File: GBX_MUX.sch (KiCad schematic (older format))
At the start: 14 parts, among them SW4 SW_DIPTRONICS_DHA-04TQ, U44 PI3DBS12212AZBSEX, U45 PI3DBS12212AZBSEX, U46 PI3DBS12212AZBSEX

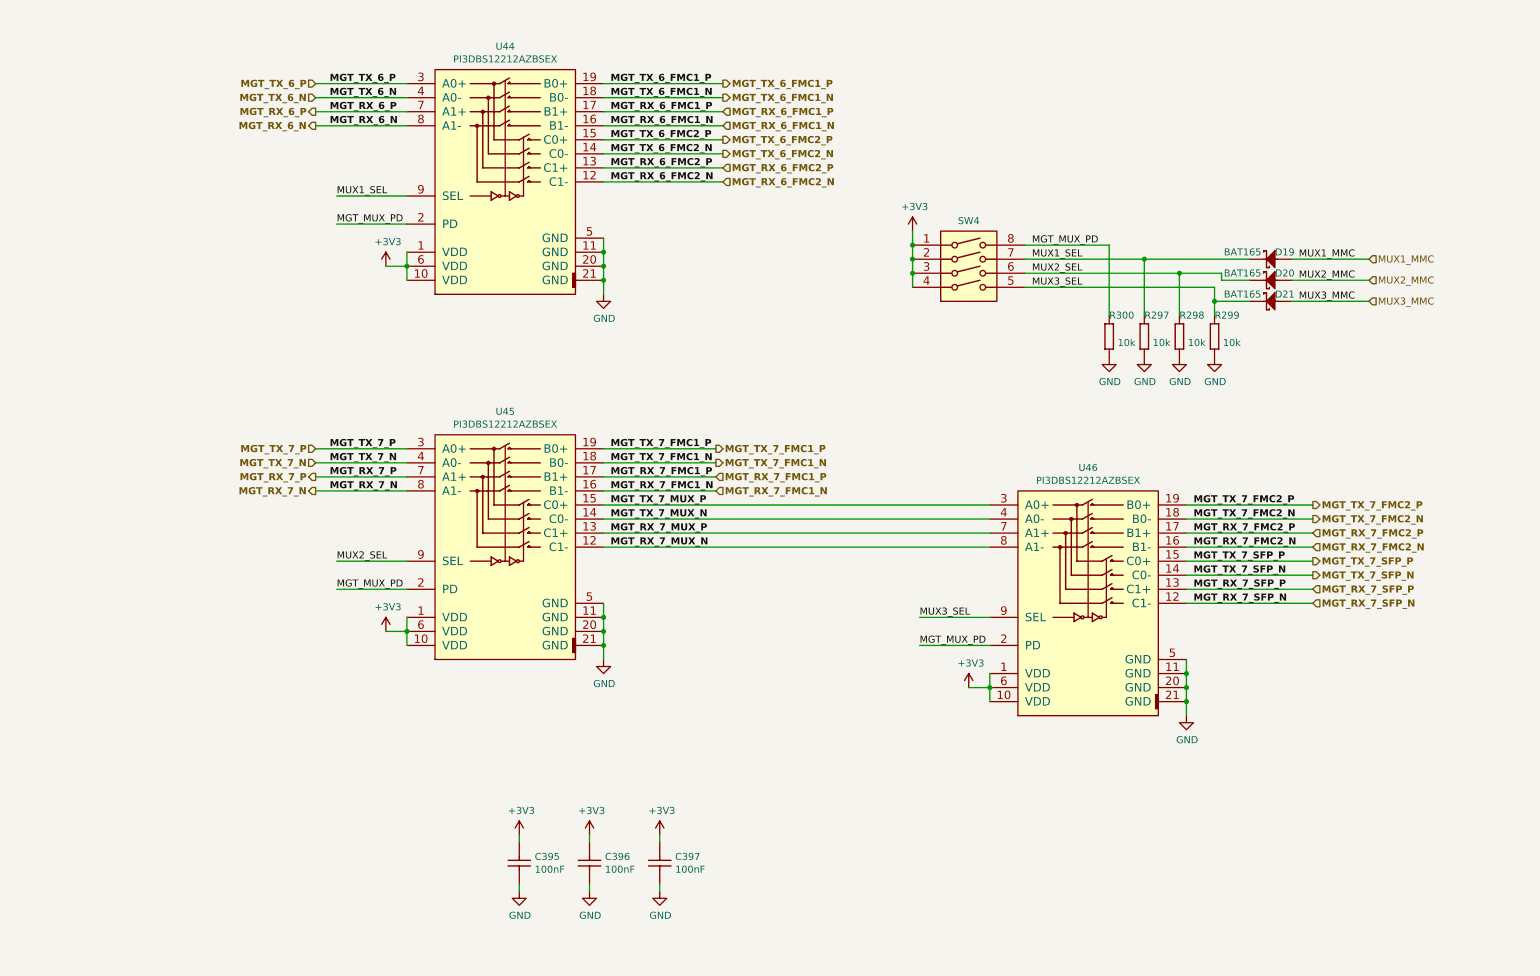
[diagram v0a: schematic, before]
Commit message: FMC HPC & LPC done, FPGA power delivery done, RGMII lines done,  MGT lines progress
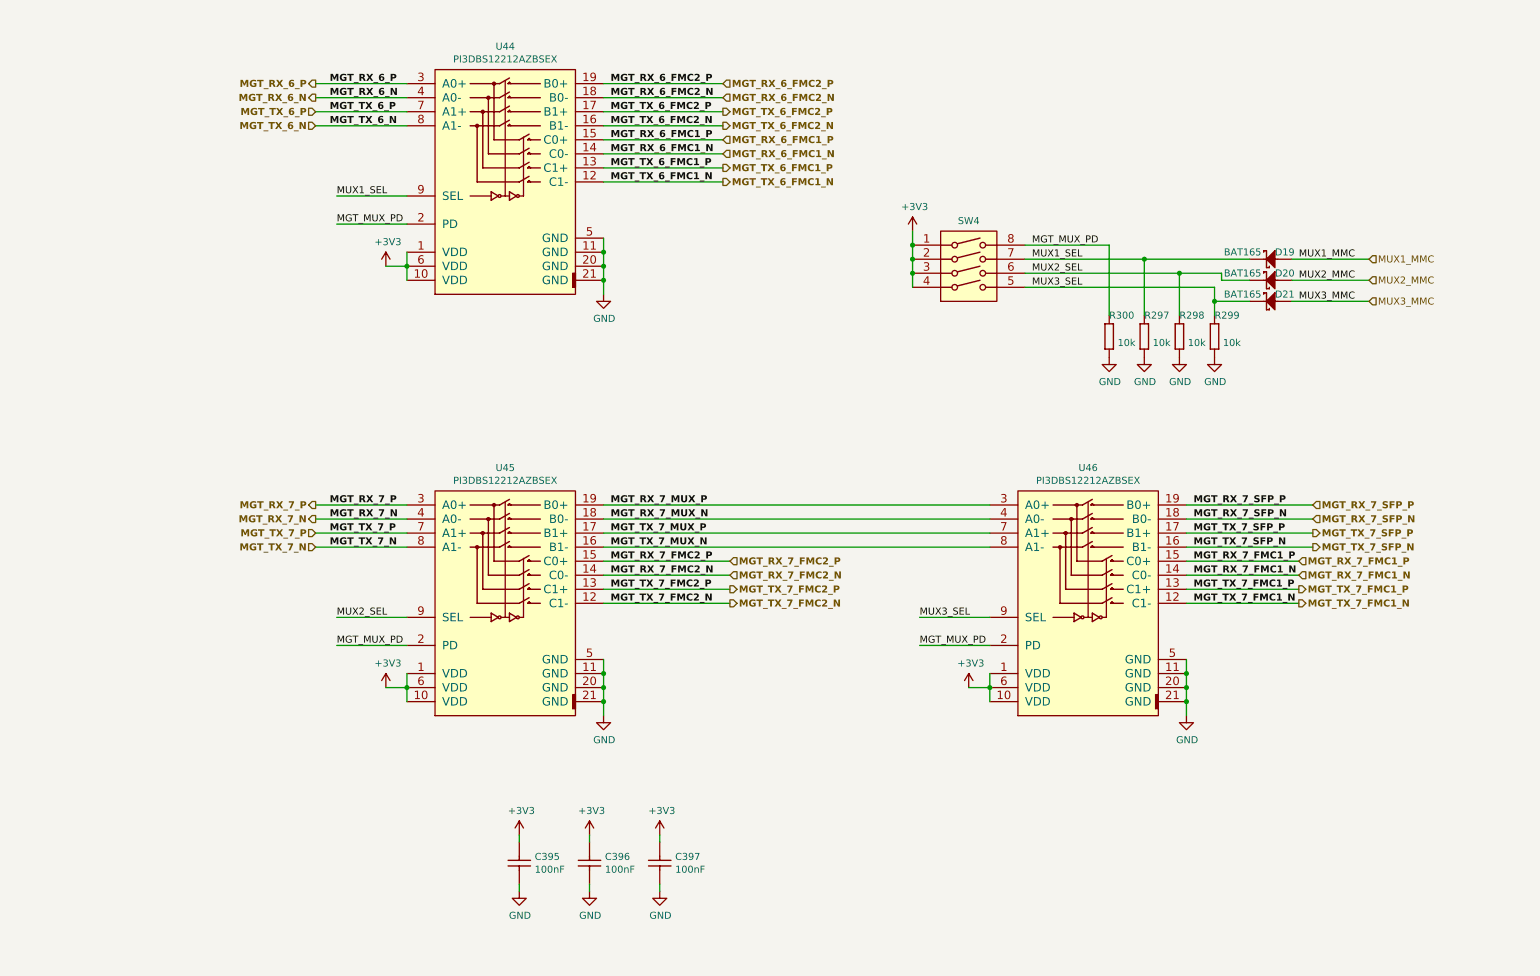
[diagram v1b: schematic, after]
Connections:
- net MGT_RX_6_FMC1_N: now also U44.14 (C0-); no longer U44.16 (B1-)
- net MGT_RX_6_FMC1_P: now also U44.15 (C0+); no longer U44.17 (B1+)
- net MGT_RX_6_FMC2_N: now also U44.18 (B0-); no longer U44.12 (C1-)
- net MGT_RX_6_FMC2_P: now also U44.19 (B0+); no longer U44.13 (C1+)
- net MGT_RX_6_N: now also U44.4 (A0-); no longer U44.8 (A1-)
- net MGT_RX_6_P: now also U44.3 (A0+); no longer U44.7 (A1+)
- net MGT_RX_7_FMC1_N: now also U46.14 (C0-); no longer U45.16 (B1-)
- net MGT_RX_7_FMC1_P: now also U46.15 (C0+); no longer U45.17 (B1+)
- net MGT_RX_7_FMC2_N: now also U45.14 (C0-); no longer U46.16 (B1-)
- net MGT_RX_7_FMC2_P: now also U45.15 (C0+); no longer U46.17 (B1+)
- net MGT_RX_7_MUX_N: now also U45.18 (B0-), U46.4 (A0-); no longer U45.12 (C1-), U46.8 (A1-)
- net MGT_RX_7_MUX_P: now also U45.19 (B0+), U46.3 (A0+); no longer U45.13 (C1+), U46.7 (A1+)
- net MGT_RX_7_N: now also U45.4 (A0-); no longer U45.8 (A1-)
- net MGT_RX_7_P: now also U45.3 (A0+); no longer U45.7 (A1+)
- net MGT_RX_7_SFP_N: now also U46.18 (B0-); no longer U46.12 (C1-)
- net MGT_RX_7_SFP_P: now also U46.19 (B0+); no longer U46.13 (C1+)
- net MGT_TX_6_FMC1_N: now also U44.12 (C1-); no longer U44.18 (B0-)
- net MGT_TX_6_FMC1_P: now also U44.13 (C1+); no longer U44.19 (B0+)
- net MGT_TX_6_FMC2_N: now also U44.16 (B1-); no longer U44.14 (C0-)
- net MGT_TX_6_FMC2_P: now also U44.17 (B1+); no longer U44.15 (C0+)
- net MGT_TX_6_N: now also U44.8 (A1-); no longer U44.4 (A0-)
- net MGT_TX_6_P: now also U44.7 (A1+); no longer U44.3 (A0+)
- net MGT_TX_7_FMC1_N: now also U46.12 (C1-); no longer U45.18 (B0-)
- net MGT_TX_7_FMC1_P: now also U46.13 (C1+); no longer U45.19 (B0+)
- net MGT_TX_7_FMC2_N: now also U45.12 (C1-); no longer U46.18 (B0-)
- net MGT_TX_7_FMC2_P: now also U45.13 (C1+); no longer U46.19 (B0+)
- net MGT_TX_7_MUX_N: now also U45.16 (B1-), U46.8 (A1-); no longer U45.14 (C0-), U46.4 (A0-)
- net MGT_TX_7_MUX_P: now also U45.17 (B1+), U46.7 (A1+); no longer U45.15 (C0+), U46.3 (A0+)
- net MGT_TX_7_N: now also U45.8 (A1-); no longer U45.4 (A0-)
- net MGT_TX_7_P: now also U45.7 (A1+); no longer U45.3 (A0+)
- net MGT_TX_7_SFP_N: now also U46.16 (B1-); no longer U46.14 (C0-)
- net MGT_TX_7_SFP_P: now also U46.17 (B1+); no longer U46.15 (C0+)
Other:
- moved on the sheet: U45

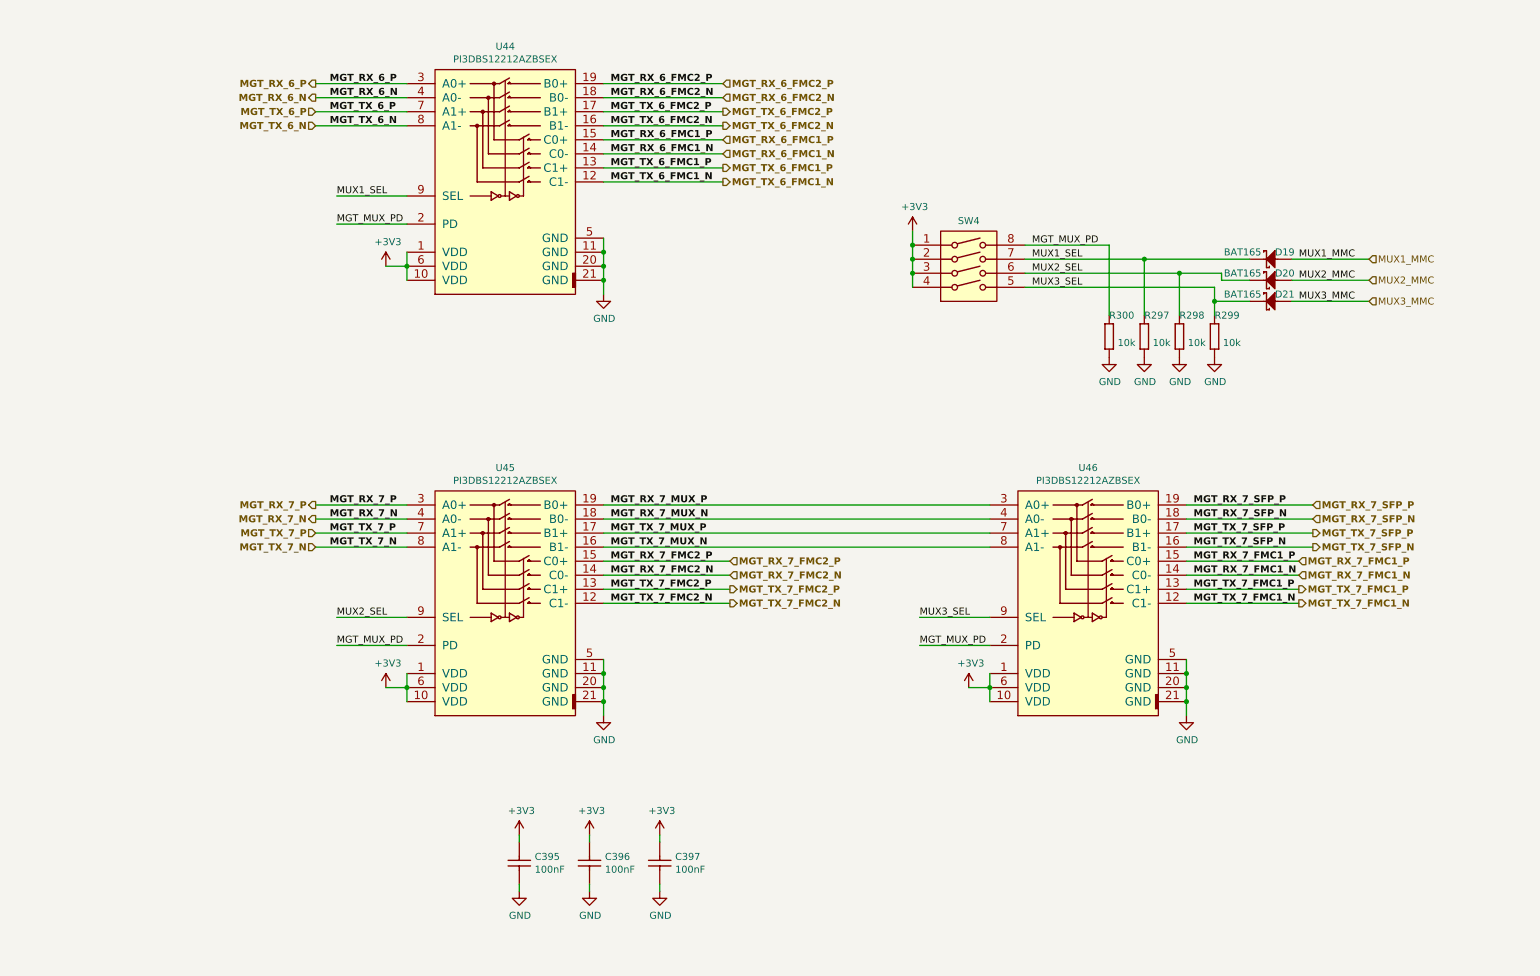
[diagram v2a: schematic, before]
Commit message: new board outline, rearranging banks connections, SODIMM memory
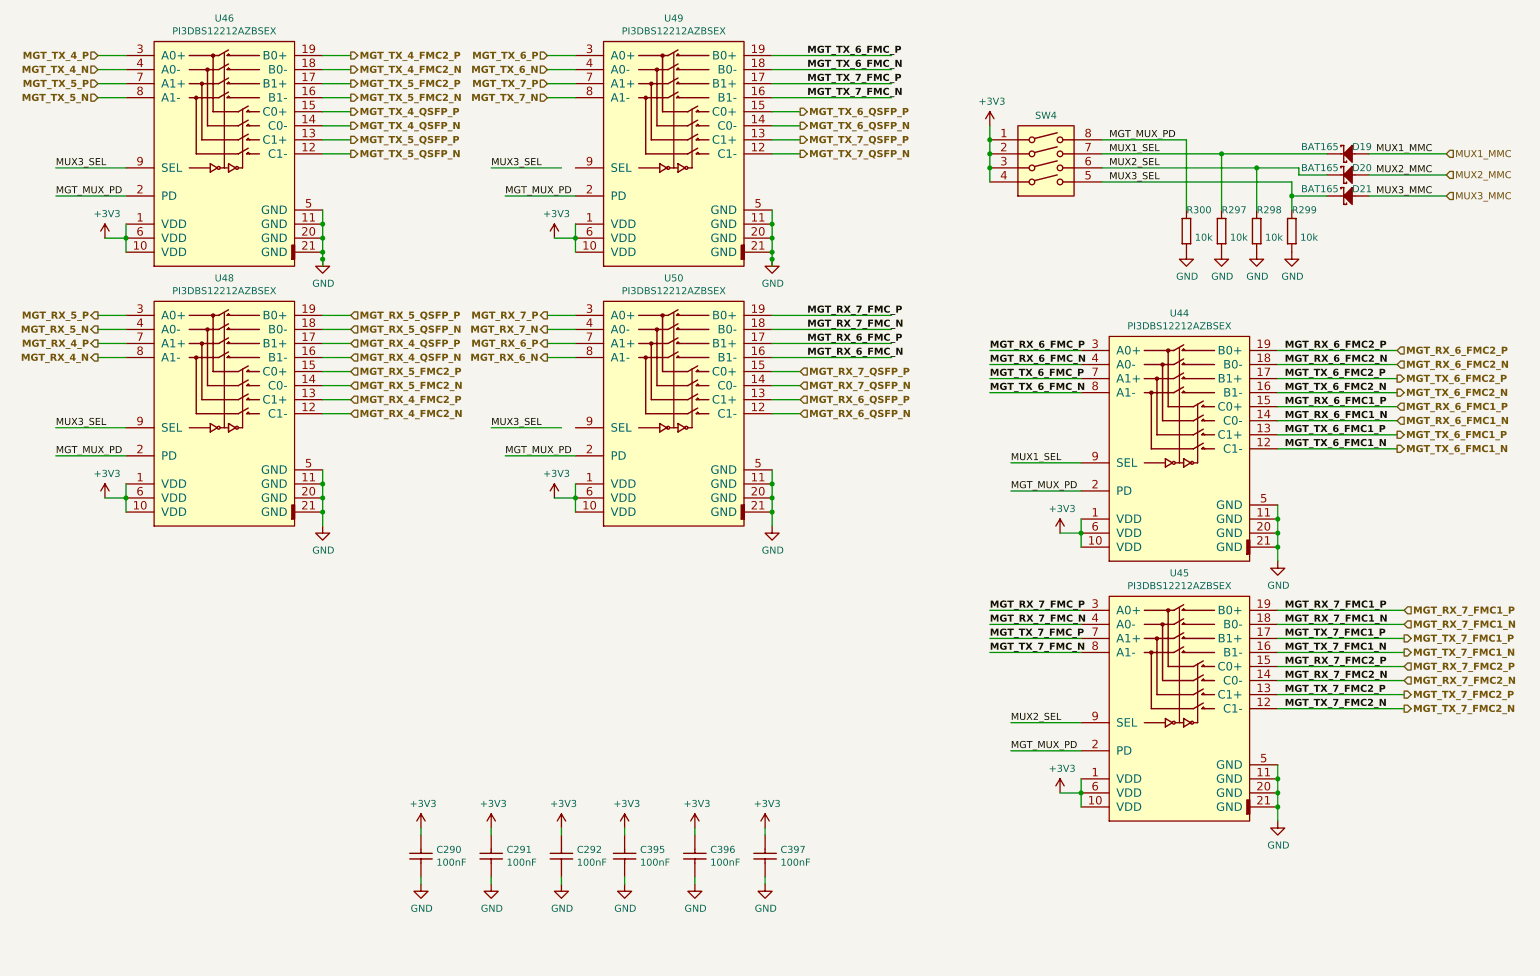
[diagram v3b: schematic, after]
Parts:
- added C290, C291, C292: CC0201_100NF_6.3V_10%_X5R, CAPC0603X33N, symbol Capacitors_SMD:CC0201_100NF_6.3V_10%_X5R
- added U48, U49, U50: PI3DBS12212AZBSEX, ICs And Semiconductors SMD:PERICOM_ZBS20, symbol Analog_&_Interface:PI3DBS12212AZBSEX
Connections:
- net labels added: MGT_RX_4_FMC2_N, MGT_RX_4_FMC2_P, MGT_RX_4_N, MGT_RX_4_P, MGT_RX_4_QSFP_N, MGT_RX_4_QSFP_P, MGT_RX_5_FMC2_N, MGT_RX_5_FMC2_P, MGT_RX_5_N, MGT_RX_5_P, MGT_RX_5_QSFP_N, MGT_RX_5_QSFP_P, MGT_RX_6_FMC_N, MGT_RX_6_FMC_P, MGT_RX_6_QSFP_N, MGT_RX_6_QSFP_P, MGT_RX_7_FMC_N, MGT_RX_7_FMC_P, MGT_RX_7_QSFP_N, MGT_RX_7_QSFP_P, MGT_TX_4_FMC2_N, MGT_TX_4_FMC2_P, MGT_TX_4_N, MGT_TX_4_P, MGT_TX_4_QSFP_N, MGT_TX_4_QSFP_P, MGT_TX_5_FMC2_N, MGT_TX_5_FMC2_P, MGT_TX_5_N, MGT_TX_5_P, MGT_TX_5_QSFP_N, MGT_TX_5_QSFP_P, MGT_TX_6_FMC_N, MGT_TX_6_FMC_P, MGT_TX_6_QSFP_N, MGT_TX_6_QSFP_P, MGT_TX_7_FMC_N, MGT_TX_7_FMC_P, MGT_TX_7_QSFP_N, MGT_TX_7_QSFP_P
- net labels removed: MGT_RX_7_MUX_N, MGT_RX_7_MUX_P, MGT_RX_7_SFP_N, MGT_RX_7_SFP_P, MGT_TX_7_MUX_N, MGT_TX_7_MUX_P, MGT_TX_7_SFP_N, MGT_TX_7_SFP_P
- wire segments 86 -> 161
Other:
- moved on the sheet: C395, C396, C397, D19, D20, D21, R297, R298, R299, R300, SW4, U44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

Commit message: routing progress
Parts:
- added C103, C104, C23, C305, C306, C37: CC0201_100NF_6.3V_10%_X5R, CAPC0603X33N, symbol Capacitors_SMD:CC0201_100NF_6.3V_10%_X5R
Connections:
- wire segments 161 -> 173
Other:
- moved on the sheet: C290, C291, C292, C395, C396, C397
